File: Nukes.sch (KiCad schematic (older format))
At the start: 30 parts, among them J5 Screw_Terminal_01x02, J6 Screw_Terminal_01x02, J7 Screw_Terminal_01x02, J8 Screw_Terminal_01x02, Q4 PMV20ENR, Q5 PMV20ENR, SW3 SW_DPDT_x2, SW4 SW_DPDT_x2, U10 LTV-817S, U9 LTV-817S

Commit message: Add files via upload
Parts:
- removed D13, D9: ARM, LED_SMD:LED_0603_1608Metric_Castellated, symbol Device:LED
- removed J5: Screw_Terminal_01x02, TerminalBlock_Phoenix:TerminalBlock_Phoenix_MPT-0,5-2-2.54_1x02_P2.54mm_Horizontal, symbol Connector:Screw_Terminal_01x02
- removed R26, R31: 470, Resistor_SMD:R_0603_1608Metric, symbol Device:R
- removed SW3, SW4: SW_DPDT_x2, Button_Switch_THT:SW_CuK_JS202011AQN_DPDT_Angled, symbol Switch:SW_DPDT_x2
- R27, R30, R32, R35: value 470 -> 1k
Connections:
- net labels added: External_Supply
- net labels removed: CONT, Fire
- wire segments 178 -> 145
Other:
- moved on the sheet: D10, D11, D12, D14, D15, D16, J6, J7, J8, JP3, JP4, Q4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

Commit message: Add files via upload
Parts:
- JP3, JP4: footprint Jumper:SolderJumper-3_P1.3mm_Open_RoundedPad1.0x1.5mm_NumberLabels -> Jumper:SolderJumper-3_P2.0mm_Open_TrianglePad1.0x1.5mm_NumberLabels
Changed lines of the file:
@@
 	1    0    0    -1
 $EndComp
-Wire Wire Line
-	900  950  900  1750
-Wire Wire Line
-	900  1750 1300 1750
-Wire Wire Line
-	1300 1750 1300 1600
-Wire Wire Line
-	1300 1600 1050 1600
-Wire Wire Line
-	1050 1600 1050 950
-Wire Wire Line
-	1050 950  900  950
-Wire Wire Line
-	1350 950  1350 1750
-Wire Wire Line
-	1350 1750 1750 1750
-Wire Wire Line
-	1750 1750 1750 950
-Wire Wire Line
-	1750 950  1600 950
-Wire Wire Line
-	1600 950  1600 1600
-Wire Wire Line
-	1600 1600 1500 1600
-Wire Wire Line
-	1500 1600 1500 950
-Wire Wire Line
-	1500 950  1350 950
-Wire Wire Line
-	2200 950  1850 950
-Wire Wire Line
-	1850 950  1850 1750
-Wire Wire Line
-	1850 1750 2200 1750
-Wire Wire Line
-	2200 1750 2200 1600
-Wire Wire Line
-	2200 1600 1950 1600
-Wire Wire Line
-	1950 1600 1950 1050
-Wire Wire Line
-	1950 1050 2200 1050
-Wire Wire Line
-	2200 1050 2200 950
-Wire Wire Line
-	2300 1750 2300 950
-Wire Wire Line
-	2300 950  2650 950
-Wire Wire Line
-	2650 950  2650 1750
-Wire Wire Line
-	2650 1750 2550 1750
-Wire Wire Line
-	2550 1750 2550 1450
-Wire Wire Line
-	2550 1450 2400 1450
-Wire Wire Line
-	2400 1450 2400 1750
-Wire Wire Line
-	2400 1750 2300 1750
-Wire Wire Line
-	2400 1350 2400 1050
-Wire Wire Line
-	2400 1050 2550 1050
-Wire Wire Line
-	2550 1050 2550 1350
-Wire Wire Line
-	2550 1350 2400 1350
-Wire Wire Line
-	3150 1750 3150 950
-Wire Wire Line
-	3150 950  3200 950
-Wire Wire Line
-	3200 950  3200 1000
-Wire Wire Line
-	3200 1000 3250 1000
-Wire Wire Line
-	3250 1000 3250 1050
-Wire Wire Line
-	3250 1050 3300 1050
-Wire Wire Line
-	3300 1050 3300 1100
-Wire Wire Line
-	3300 1100 3350 1100
-Wire Wire Line
-	3350 1100 3350 1150
-Wire Wire Line
-	3350 1150 3400 1150
-Wire Wire Line
-	3400 1150 3400 1200
-Wire Wire Line
-	3400 1200 3450 1200
-Wire Wire Line
-	3450 1200 3450 1250
-Wire Wire Line
-	3450 1250 3500 1250
-Wire Wire Line
-	3500 1250 3500 1300
-Wire Wire Line
-	3500 1300 3550 1300
-Wire Wire Line
-	3550 1300 3550 1400
-Wire Wire Line
-	3550 1400 3600 1400
-Wire Wire Line
-	3600 1400 3600 1500
-Wire Wire Line
-	3600 1500 3650 1500
-Wire Wire Line
-	3650 950  3800 950
-Wire Wire Line
-	3800 1750 3600 1750
-Wire Wire Line
-	3600 1750 3600 1550
-Wire Wire Line
-	3600 1550 3500 1550
-Wire Wire Line
-	3500 1550 3500 1450
-Wire Wire Line
-	3500 1450 3400 1450
-Wire Wire Line
-	3400 1450 3400 1350
-Wire Wire Line
-	3400 1350 3350 1350
-Wire Wire Line
-	3350 1350 3350 1250
-Wire Wire Line
-	3350 1250 3250 1250
-Wire Wire Line
-	3650 950  3650 1500
-Wire Wire Line
-	3800 950  3800 1750
-Wire Wire Line
-	3250 1150 3250 1250
-Connection ~ 3650 1500
-Wire Wire Line
-	3650 1500 3650 1550
-Connection ~ 3250 1250
-Wire Wire Line
-	3250 1250 3250 1750
-Wire Wire Line
-	3950 1000 3950 1750
-Wire Wire Line
-	3950 1750 4100 1750
-Wire Wire Line
-	4100 1750 4100 1000
-Wire Wire Line
-	4100 1000 3950 1000
-Wire Wire Line
-	4550 1000 4250 1000
-Wire Wire Line
-	4250 1000 4250 1700
-Wire Wire Line
-	4250 1700 4600 1700
-Wire Wire Line
-	4600 1700 4600 1600
-Wire Wire Line
-	4600 1600 4350 1600
-Wire Wire Line
-	4350 1600 4350 1100
-Wire Wire Line
-	4350 1100 4550 1100
-Wire Wire Line
-	4550 1100 4550 1000
-Wire Wire Line
-	4700 1000 5100 1000
-Wire Wire Line
-	5100 1000 5100 1700
-Wire Wire Line
-	5100 1700 4700 1700
-Wire Wire Line
-	4700 1700 4700 1000
-Wire Wire Line
-	4800 1100 5000 1100
-Wire Wire Line
-	5000 1100 5000 1600
-Wire Wire Line
-	5000 1600 4800 1600
-Wire Wire Line
-	4800 1600 4800 1100
-Wire Wire Line
-	3150 1750 3250 1750
 $Comp
 L Connector:Screw_Terminal_01x02 J?
@@
 F 0 "JP4" H 7550 4005 50  0000 C CNN
 F 1 "SolderJumper_3_Open" H 7550 3914 50  0000 C CNN
-F 2 "Jumper:SolderJumper-3_P1.3mm_Open_RoundedPad1.0x1.5mm_NumberLabels" H 7550 3800 50  0001 C CNN
+F 2 "Jumper:SolderJumper-3_P2.0mm_Open_TrianglePad1.0x1.5mm_NumberLabels" H 7550 3800 50  0001 C CNN
 F 3 "~" H 7550 3800 50  0001 C CNN
 	1    7550 3800
@@
 F 0 "JP3" H 3250 4155 50  0000 C CNN
 F 1 "SolderJumper_3_Open" H 3250 4064 50  0000 C CNN
-F 2 "Jumper:SolderJumper-3_P1.3mm_Open_RoundedPad1.0x1.5mm_NumberLabels" H 3250 3950 50  0001 C CNN
+F 2 "Jumper:SolderJumper-3_P2.0mm_Open_TrianglePad1.0x1.5mm_NumberLabels" H 3250 3950 50  0001 C CNN
 F 3 "~" H 3250 3950 50  0001 C CNN
 	1    3250 3950

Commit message: pcb update
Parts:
- removed JP3, JP4: SolderJumper_3_Open, Jumper:SolderJumper-3_P2.0mm_Open_TrianglePad1.0x1.5mm_NumberLabels, symbol Jumper:SolderJumper_3_Open
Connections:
- net External_Supply: now also D10.2 (A), D14.2 (A), J6.1 (Pin_1), J8.1 (Pin_1)
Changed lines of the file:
@@
 Wire Wire Line
 	9150 4800 8900 4800
-$Comp
-L Jumper:SolderJumper_3_Open JP?
-U 1 1 5DE04B45
-P 7550 3800
-AR Path="/5DDE6CFA/5DE04B45" Ref="JP?"  Part="1"
-AR Path="/5DDE1103/5DE04B45" Ref="JP4"  Part="1"
-F 0 "JP4" H 7550 4005 50  0000 C CNN
-F 1 "SolderJumper_3_Open" H 7550 3914 50  0000 C CNN
-F 2 "Jumper:SolderJumper-3_P2.0mm_Open_TrianglePad1.0x1.5mm_NumberLabels" H 7550 3800 50  0001 C CNN
-F 3 "~" H 7550 3800 50  0001 C CNN
-	1    7550 3800
-	1    0    0    -1
-$EndComp
-Wire Wire Line
-	7750 3800 7950 3800
-Wire Wire Line
-	7950 3800 7950 3650
 Text Notes 4800 2500 0    50   ~ 0
 External ematch supply
@@
 $Comp
 L power:+3V3 #PWR?
-U 1 1 5DE04B74
-P 7950 3650
-AR Path="/5DDE6CFA/5DE04B74" Ref="#PWR?"  Part="1"
-AR Path="/5DDE1103/5DE04B74" Ref="#PWR061"  Part="1"
-F 0 "#PWR061" H 7950 3500 50  0001 C CNN
-F 1 "+3V3" H 7965 3823 50  0000 C CNN
-F 2 "" H 7950 3650 50  0001 C CNN
-F 3 "" H 7950 3650 50  0001 C CNN
-	1    7950 3650
-	1    0    0    -1
-$EndComp
-$Comp
-L power:+3V3 #PWR?
 U 1 1 5DE04B7A
 P 9150 4600
@@
 Wire Wire Line
 	4900 4950 4650 4950
-$Comp
-L Jumper:SolderJumper_3_Open JP?
-U 1 1 5DE32382
-P 3250 3950
-AR Path="/5DDE6CFA/5DE32382" Ref="JP?"  Part="1"
-AR Path="/5DDE1103/5DE32382" Ref="JP3"  Part="1"
-F 0 "JP3" H 3250 4155 50  0000 C CNN
-F 1 "SolderJumper_3_Open" H 3250 4064 50  0000 C CNN
-F 2 "Jumper:SolderJumper-3_P2.0mm_Open_TrianglePad1.0x1.5mm_NumberLabels" H 3250 3950 50  0001 C CNN
-F 3 "~" H 3250 3950 50  0001 C CNN
-	1    3250 3950
-	1    0    0    -1
-$EndComp
-Wire Wire Line
-	3450 3950 3650 3950
-Wire Wire Line
-	3650 3950 3650 3800
 $Comp
 L Device:D_Schottky D?
@@
 $Comp
 L power:+3V3 #PWR?
-U 1 1 5DE323B1
-P 3650 3800
-AR Path="/5DDE6CFA/5DE323B1" Ref="#PWR?"  Part="1"
-AR Path="/5DDE1103/5DE323B1" Ref="#PWR054"  Part="1"
-F 0 "#PWR054" H 3650 3650 50  0001 C CNN
-F 1 "+3V3" H 3665 3973 50  0000 C CNN
-F 2 "" H 3650 3800 50  0001 C CNN
-F 3 "" H 3650 3800 50  0001 C CNN
-	1    3650 3800
-	1    0    0    -1
-$EndComp
-$Comp
-L power:+3V3 #PWR?
 U 1 1 5DE323B7
 P 4900 4750
@@
 Wire Wire Line
 	3800 4150 3250 4150
-Wire Wire Line
-	3250 4150 3250 4100
 Connection ~ 3800 4150
 Wire Wire Line
 	8050 4000 7550 4000
-Wire Wire Line
-	7550 4000 7550 3950
 Connection ~ 8050 4000
 Wire Wire Line
@@
 Wire Wire Line
 	5450 2600 6100 2600
-Wire Wire Line
-	7350 3800 6850 3800
-Wire Wire Line
-	2350 3950 3050 3950
-Text Label 2350 3950 0    50   ~ 0
+Text Label 3250 4150 0    50   ~ 0
 External_Supply
-Text Label 6850 3800 0    50   ~ 0
+Text Label 7550 4000 0    50   ~ 0
 External_Supply
 $EndSCHEMATC

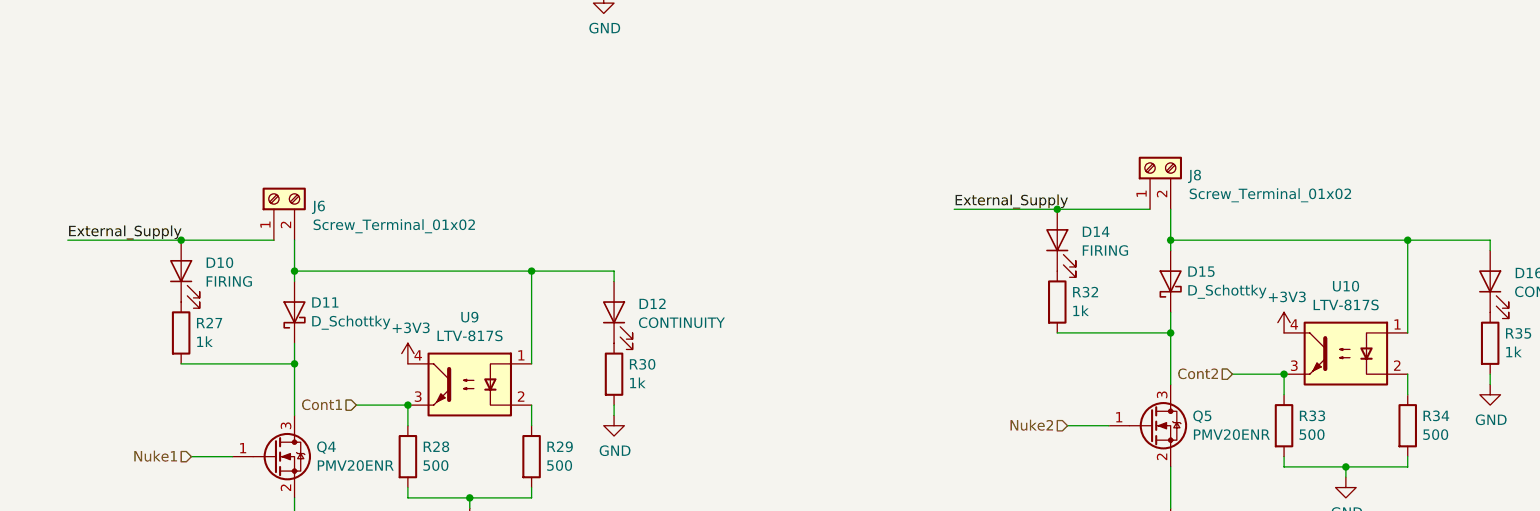
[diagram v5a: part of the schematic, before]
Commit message: replaced screw terminals with ramps connectors
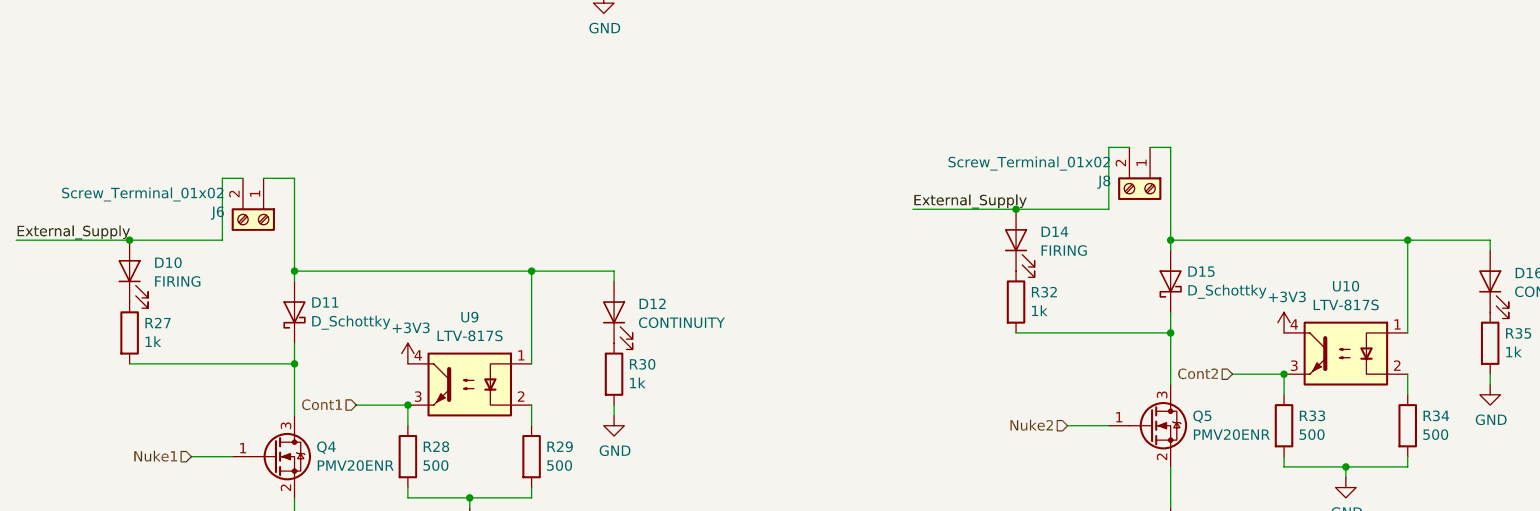
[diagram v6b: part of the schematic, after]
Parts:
- J6, J8: footprint TerminalBlock_Phoenix:TerminalBlock_Phoenix_MPT-0,5-2-2.54_1x02_P2.54mm_Horizontal -> iclr-hw:PHOENIX_1757242
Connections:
- net External_Supply: now also J6.2 (Pin_2), J8.2 (Pin_2); no longer J6.1 (Pin_1), J8.1 (Pin_1)
- net at D15.2 (A), D16.2 (A), U10.1: now also J8.1 (Pin_1); no longer J8.2 (Pin_2)
- net at D11.2 (A), D12.2 (A), U9.1: now also J6.1 (Pin_1); no longer J6.2 (Pin_2)
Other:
- moved on the sheet: D10, D14, J6, J8, R27, R32
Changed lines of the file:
@@
 L Connector:Screw_Terminal_01x02 J?
 U 1 1 5DE04AFB
-P 8500 3800
+P 8500 3900
 AR Path="/5DDE6CFA/5DE04AFB" Ref="J?"  Part="1"
 AR Path="/5DDE1103/5DE04AFB" Ref="J8"  Part="1"
-F 0 "J8" V 8464 3612 50  0000 R CNN
-F 1 "Screw_Terminal_01x02" V 8373 3612 50  0000 R CNN
-F 2 "TerminalBlock_Phoenix:TerminalBlock_Phoenix_MPT-0,5-2-2.54_1x02_P2.54mm_Horizontal" H 8500 3800 50  0001 C CNN
-F 3 "~" H 8500 3800 50  0001 C CNN
-	1    8500 3800
-	0    -1   -1   0
+F 0 "J8" V 8464 3712 50  0000 R CNN
+F 1 "Screw_Terminal_01x02" V 8373 3712 50  0000 R CNN
+F 2 "iclr-hw:PHOENIX_1757242" H 8500 3900 50  0001 C CNN
+F 3 "~" H 8500 3900 50  0001 C CNN
+	1    8500 3900
+	0    1    1    0
 $EndComp
 $Comp
 L Device:R R?
 U 1 1 5DE04B01
-P 8050 4450
+P 7850 4450
 AR Path="/5DDE6CFA/5DE04B01" Ref="R?"  Part="1"
 AR Path="/5DDE1103/5DE04B01" Ref="R32"  Part="1"
-F 0 "R32" H 8120 4496 50  0000 L CNN
-F 1 "1k" H 8120 4405 50  0000 L CNN
-F 2 "Resistor_SMD:R_0603_1608Metric" V 7980 4450 50  0001 C CNN
-F 3 "~" H 8050 4450 50  0001 C CNN
-	1    8050 4450
+F 0 "R32" H 7920 4496 50  0000 L CNN
+F 1 "1k" H 7920 4405 50  0000 L CNN
+F 2 "Resistor_SMD:R_0603_1608Metric" V 7780 4450 50  0001 C CNN
+F 3 "~" H 7850 4450 50  0001 C CNN
+	1    7850 4450
 	1    0    0    -1
 $EndComp
@@
 L Device:LED D?
 U 1 1 5DE04B07
-P 8050 4150
+P 7850 4150
 AR Path="/5DDE6CFA/5DE04B07" Ref="D?"  Part="1"
 AR Path="/5DDE1103/5DE04B07" Ref="D14"  Part="1"
-F 0 "D14" V 8089 4033 50  0000 R CNN
-F 1 "FIRING" V 7998 4033 50  0000 R CNN
-F 2 "LED_SMD:LED_0603_1608Metric_Castellated" H 8050 4150 50  0001 C CNN
-F 3 "~" H 8050 4150 50  0001 C CNN
-	1    8050 4150
+F 0 "D14" V 7889 4033 50  0000 R CNN
+F 1 "FIRING" V 7798 4033 50  0000 R CNN
+F 2 "LED_SMD:LED_0603_1608Metric_Castellated" H 7850 4150 50  0001 C CNN
+F 3 "~" H 7850 4150 50  0001 C CNN
+	1    7850 4150
 	0    -1   -1   0
 $EndComp
 Wire Wire Line
-	8050 4000 8500 4000
-Wire Wire Line
-	8600 4500 8600 4600
-Wire Wire Line
-	8050 4600 8600 4600
-Connection ~ 8600 4600
-Wire Wire Line
-	8600 4600 8600 4850
-Wire Wire Line
-	8600 4000 8600 4150
+	7850 4000 8300 4000
 $Comp
 L Device:Q_NMOS_GSD Q?
@@
 L Connector:Screw_Terminal_01x02 J?
 U 1 1 5DE32338
-P 4250 3950
+P 4200 4050
 AR Path="/5DDE6CFA/5DE32338" Ref="J?"  Part="1"
 AR Path="/5DDE1103/5DE32338" Ref="J6"  Part="1"
-F 0 "J6" V 4214 3762 50  0000 R CNN
-F 1 "Screw_Terminal_01x02" V 4123 3762 50  0000 R CNN
-F 2 "TerminalBlock_Phoenix:TerminalBlock_Phoenix_MPT-0,5-2-2.54_1x02_P2.54mm_Horizontal" H 4250 3950 50  0001 C CNN
-F 3 "~" H 4250 3950 50  0001 C CNN
-	1    4250 3950
-	0    -1   -1   0
+F 0 "J6" V 4164 3862 50  0000 R CNN
+F 1 "Screw_Terminal_01x02" V 4073 3862 50  0000 R CNN
+F 2 "iclr-hw:PHOENIX_1757242" H 4200 4050 50  0001 C CNN
+F 3 "~" H 4200 4050 50  0001 C CNN
+	1    4200 4050
+	0    1    1    0
 $EndComp
 $Comp
 L Device:R R?
 U 1 1 5DE3233E
-P 3800 4600
+P 3550 4600
 AR Path="/5DDE6CFA/5DE3233E" Ref="R?"  Part="1"
 AR Path="/5DDE1103/5DE3233E" Ref="R27"  Part="1"
-F 0 "R27" H 3870 4646 50  0000 L CNN
-F 1 "1k" H 3870 4555 50  0000 L CNN
-F 2 "Resistor_SMD:R_0603_1608Metric" V 3730 4600 50  0001 C CNN
-F 3 "~" H 3800 4600 50  0001 C CNN
-	1    3800 4600
+F 0 "R27" H 3620 4646 50  0000 L CNN
+F 1 "1k" H 3620 4555 50  0000 L CNN
+F 2 "Resistor_SMD:R_0603_1608Metric" V 3480 4600 50  0001 C CNN
+F 3 "~" H 3550 4600 50  0001 C CNN
+	1    3550 4600
 	1    0    0    -1
 $EndComp
@@
 L Device:LED D?
 U 1 1 5DE32344
-P 3800 4300
+P 3550 4300
 AR Path="/5DDE6CFA/5DE32344" Ref="D?"  Part="1"
 AR Path="/5DDE1103/5DE32344" Ref="D10"  Part="1"
-F 0 "D10" V 3839 4183 50  0000 R CNN
-F 1 "FIRING" V 3748 4183 50  0000 R CNN
-F 2 "LED_SMD:LED_0603_1608Metric_Castellated" H 3800 4300 50  0001 C CNN
-F 3 "~" H 3800 4300 50  0001 C CNN
-	1    3800 4300
+F 0 "D10" V 3589 4183 50  0000 R CNN
+F 1 "FIRING" V 3498 4183 50  0000 R CNN
+F 2 "LED_SMD:LED_0603_1608Metric_Castellated" H 3550 4300 50  0001 C CNN
+F 3 "~" H 3550 4300 50  0001 C CNN
+	1    3550 4300
 	0    -1   -1   0
 $EndComp
 Wire Wire Line
-	3800 4150 4250 4150
-Wire Wire Line
-	4350 4650 4350 4750
-Wire Wire Line
-	3800 4750 4350 4750
-Connection ~ 4350 4750
-Wire Wire Line
-	4350 4750 4350 5000
-Wire Wire Line
-	4350 4150 4350 4300
+	3550 4150 4000 4150
 $Comp
 L Device:Q_NMOS_GSD Q?
@@
 Cont2
 Wire Wire Line
-	3800 4150 3250 4150
-Connection ~ 3800 4150
-Wire Wire Line
-	8050 4000 7550 4000
-Connection ~ 8050 4000
+	3550 4150 3000 4150
+Connection ~ 3550 4150
+Wire Wire Line
+	7850 4000 7350 4000
+Connection ~ 7850 4000
 Wire Wire Line
 	5450 2700 5850 2700
@@
 Wire Wire Line
 	5450 2600 6100 2600
-Text Label 3250 4150 0    50   ~ 0
+Text Label 3000 4150 0    50   ~ 0
 External_Supply
-Text Label 7550 4000 0    50   ~ 0
+Text Label 7350 4000 0    50   ~ 0
 External_Supply
+Wire Wire Line
+	8600 4500 8600 4600
+Wire Wire Line
+	7850 4600 8600 4600
+Connection ~ 8600 4600
+Wire Wire Line
+	8600 4600 8600 4850
+Wire Wire Line
+	8300 4000 8300 3700
+Wire Wire Line
+	8300 3700 8400 3700
+Wire Wire Line
+	8600 3700 8500 3700
+Wire Wire Line
+	8600 3700 8600 4150
+Wire Wire Line
+	4350 4650 4350 4750
+Wire Wire Line
+	3550 4750 4350 4750
+Connection ~ 4350 4750
+Wire Wire Line
+	4350 4750 4350 5000
+Wire Wire Line
+	4350 3850 4200 3850
+Wire Wire Line
+	4350 3850 4350 4300
+Wire Wire Line
+	4100 3850 4000 3850
+Wire Wire Line
+	4000 3850 4000 4150
 $EndSCHEMATC

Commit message: shroom
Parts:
- J7: footprint TerminalBlock_Phoenix:TerminalBlock_Phoenix_MPT-0,5-2-2.54_1x02_P2.54mm_Horizontal -> iclr-hw:PHOENIX_1757242
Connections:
- net External_Supply: now also J7.2 (Pin_2); no longer J7.1 (Pin_1)
- net GND: now also J7.1 (Pin_1); no longer J7.2 (Pin_2)
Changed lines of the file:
@@
 F 0 "J7" H 5168 2275 50  0000 C CNN
 F 1 "Screw_Terminal_01x02" H 5168 2366 50  0000 C CNN
-F 2 "TerminalBlock_Phoenix:TerminalBlock_Phoenix_MPT-0,5-2-2.54_1x02_P2.54mm_Horizontal" H 5250 2600 50  0001 C CNN
+F 2 "iclr-hw:PHOENIX_1757242" H 5250 2600 50  0001 C CNN
 F 3 "~" H 5250 2600 50  0001 C CNN
 	1    5250 2600
@@
 Connection ~ 7850 4000
 Wire Wire Line
-	5450 2700 5850 2700
-Wire Wire Line
-	5850 2700 5850 2950
+	6350 2600 6350 2850
 $Comp
 L power:GND #PWR0101
 U 1 1 5DEC1515
-P 5850 2950
-F 0 "#PWR0101" H 5850 2700 50  0001 C CNN
-F 1 "GND" H 5855 2777 50  0000 C CNN
-F 2 "" H 5850 2950 50  0001 C CNN
-F 3 "" H 5850 2950 50  0001 C CNN
-	1    5850 2950
-	1    0    0    -1
-$EndComp
-Text Label 6100 2600 2    50   ~ 0
+P 6350 2850
+F 0 "#PWR0101" H 6350 2600 50  0001 C CNN
+F 1 "GND" H 6355 2677 50  0000 C CNN
+F 2 "" H 6350 2850 50  0001 C CNN
+F 3 "" H 6350 2850 50  0001 C CNN
+	1    6350 2850
+	1    0    0    -1
+$EndComp
+Text Label 6100 2700 2    50   ~ 0
 External_Supply
 Wire Wire Line
-	5450 2600 6100 2600
+	5450 2700 6100 2700
 Text Label 3000 4150 0    50   ~ 0
 External_Supply
@@
 Wire Wire Line
 	4000 3850 4000 4150
+Wire Wire Line
+	5450 2600 6350 2600
 $EndSCHEMATC
